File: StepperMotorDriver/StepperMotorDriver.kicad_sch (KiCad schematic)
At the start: 1 part, among them U1 A4988SETTR-T

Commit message: edited schematic
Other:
- note added: "Record to Beat: 0.6"x0.8" 15mm x 20.23mm"
- moved on the sheet: U1
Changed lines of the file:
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@@
 	(generator_version "8.0")
 	(paper "A5")
+	(text "Record to Beat: \n0.6\"x0.8\"\n15mm x 20.23mm"
+		(exclude_from_sim no)
+		(at 185.674 19.812 0)
+		(effects
+			(font
+				(size 1.27 1.27)
+			)
+		)
+	)
 	(symbol
 		(lib_id "Project_Symbols:A4988SETTR-T")
-		(at 83.82 44.45 0)
+		(at 81.28 41.91 0)
 		(unit 1)
 		(exclude_from_sim no)
@@
 		(fields_autoplaced yes)
 		(property "Reference" "U1"
-			(at 102.4318 35.56 0)
+			(at 99.8918 33.02 0)
 			(effects
 				(font
@@
 		)
 		(property "Value" "A4988SETTR-T"
-			(at 102.4318 38.1 0)
+			(at 99.8918 35.56 0)
 			(effects
 				(font
@@
 		)
 		(property "Footprint" "QFN-28_ALM"
-			(at 101.6 41.91 0)
+			(at 99.06 39.37 0)
 			(effects
 				(font
@@
 		)
 		(property "Datasheet" "A4988SETTR-T"
-			(at 101.6 39.37 0)
+			(at 99.06 36.83 0)
 			(effects
 				(font
@@
 		)
 		(property "Description" ""
-			(at 83.82 44.45 0)
+			(at 81.28 41.91 0)
 			(effects
 				(font

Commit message: Edited Schematic
Changed main IC symbol
Added Peripheral components
Assigned footprints
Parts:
- added C1, C2, C3, C4: C, symbol Device:C
- added C5: 100u, symbol Device:C_Polarized
- added R1, R2, R3, R4: R_US, symbol Device:R_US
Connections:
- net at U1.13 (ROSC): now also R2.2
- net at U1.14 (~{SLEEP}): now also R1.2
- net +3.3V: now reaches U1.15 (VDD)
- net +3.3V: now also C4.1, R1.1
- net GND: now reaches U1.18 (GND)
- net GND: now also U1.29 (GND), U1.3 (GND), C1.1, C4.2, C5.2, R2.1, R3.2, R4.2
- net at U1.20 (NC): now also U1.25 (NC), U1.7 (NC)
- net +24V: now reaches U1.22 (VBB1)
- net +24V: now also U1.28 (VBB2), C2.2, C5.1
- net at U1.23 (SENSE1): now also R4.1
- net at U1.27 (SENSE2): now also R3.1
- net at U1.4 (CP1): now also C3.2
- net at U1.5 (CP2): now also C3.1
- net at U1.6 (VCP): now also C2.1
- net at U1.8 (VREG): now also C1.2

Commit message: Updated Schematic
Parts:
- removed R2: R_US, symbol Device:R_US
- added J1: Conn_01x04_Pin, symbol Connector:Conn_01x04_Pin
- added J2: Conn_01x03_Pin, symbol Connector:Conn_01x03_Pin
- C1, C4: value C -> 0.22u
- C2, C3: value C -> 0.1u
- R1: value R_US -> 5k
- R3, R4: value R_US -> 68m
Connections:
- net GND: now also U1.13 (ROSC)
- net at U1.1 (OUT2B): now also J1.4 (Pin_4)
- net MS2: now reaches U1.10 (MS2)
- net MS2: now also J2.2 (Pin_2)
- net MS3: now reaches U1.11 (MS3)
- net MS3: now also J2.3 (Pin_3)
- net at U1.21 (OUT1B): now also J1.2 (Pin_2)
- net at U1.24 (OUT1A): now also J1.1 (Pin_1)
- net at U1.26 (OUT2A): now also J1.3 (Pin_3)
- net MS1: now reaches U1.9 (MS1)
- net MS1: now also J2.1 (Pin_1)
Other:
- moved on the sheet: C4, R1

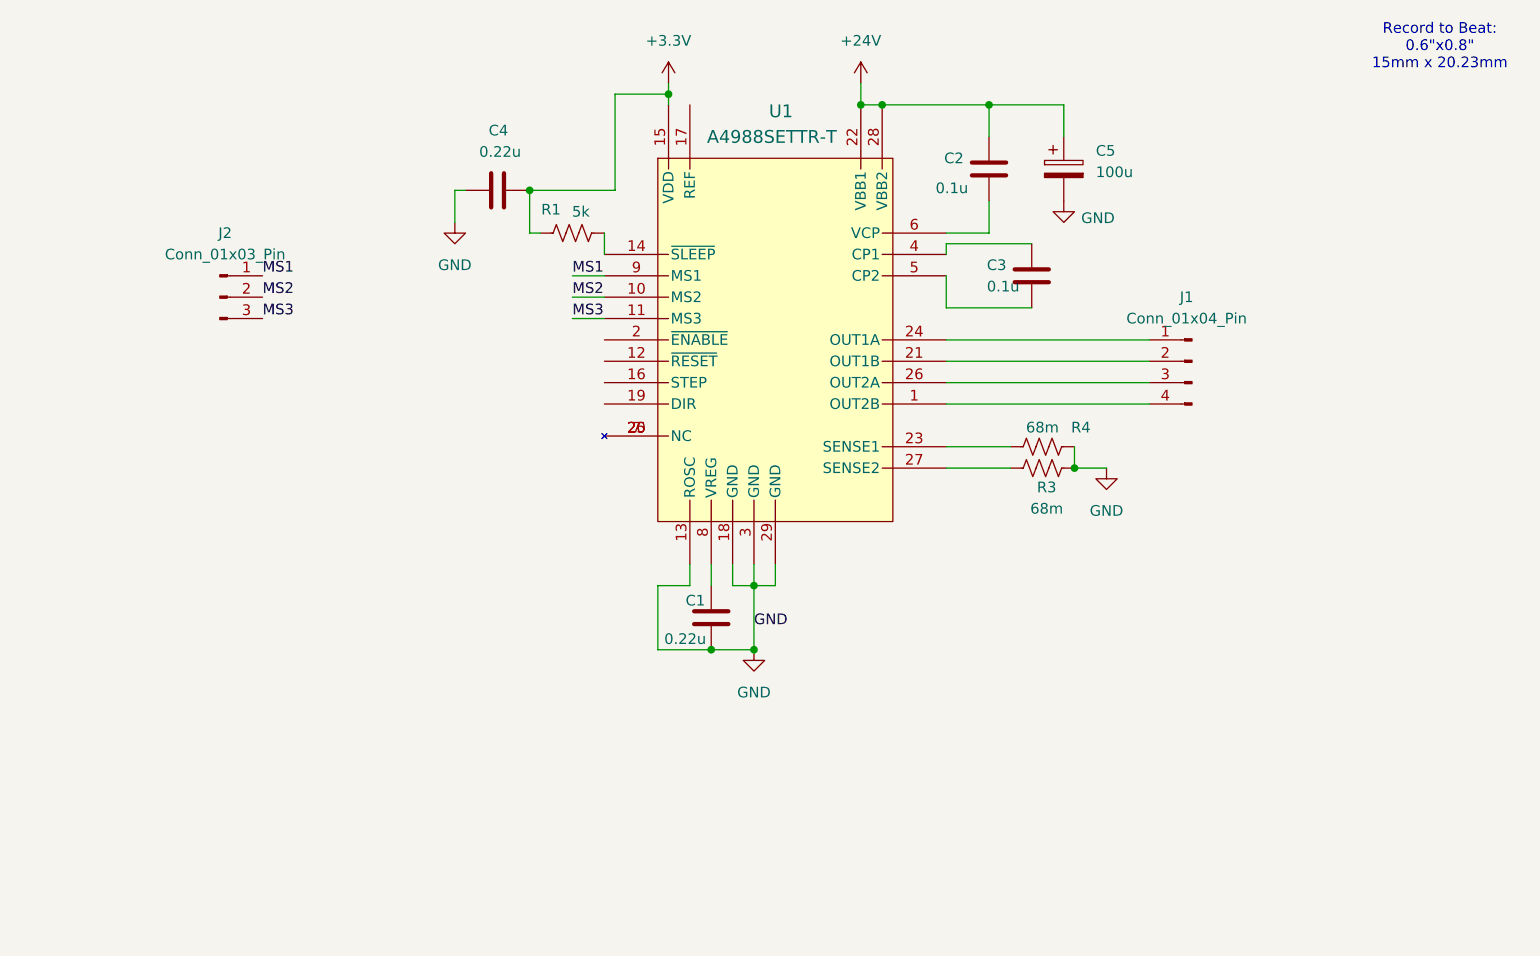
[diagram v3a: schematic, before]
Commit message: COMPLETED schematic and added documentation
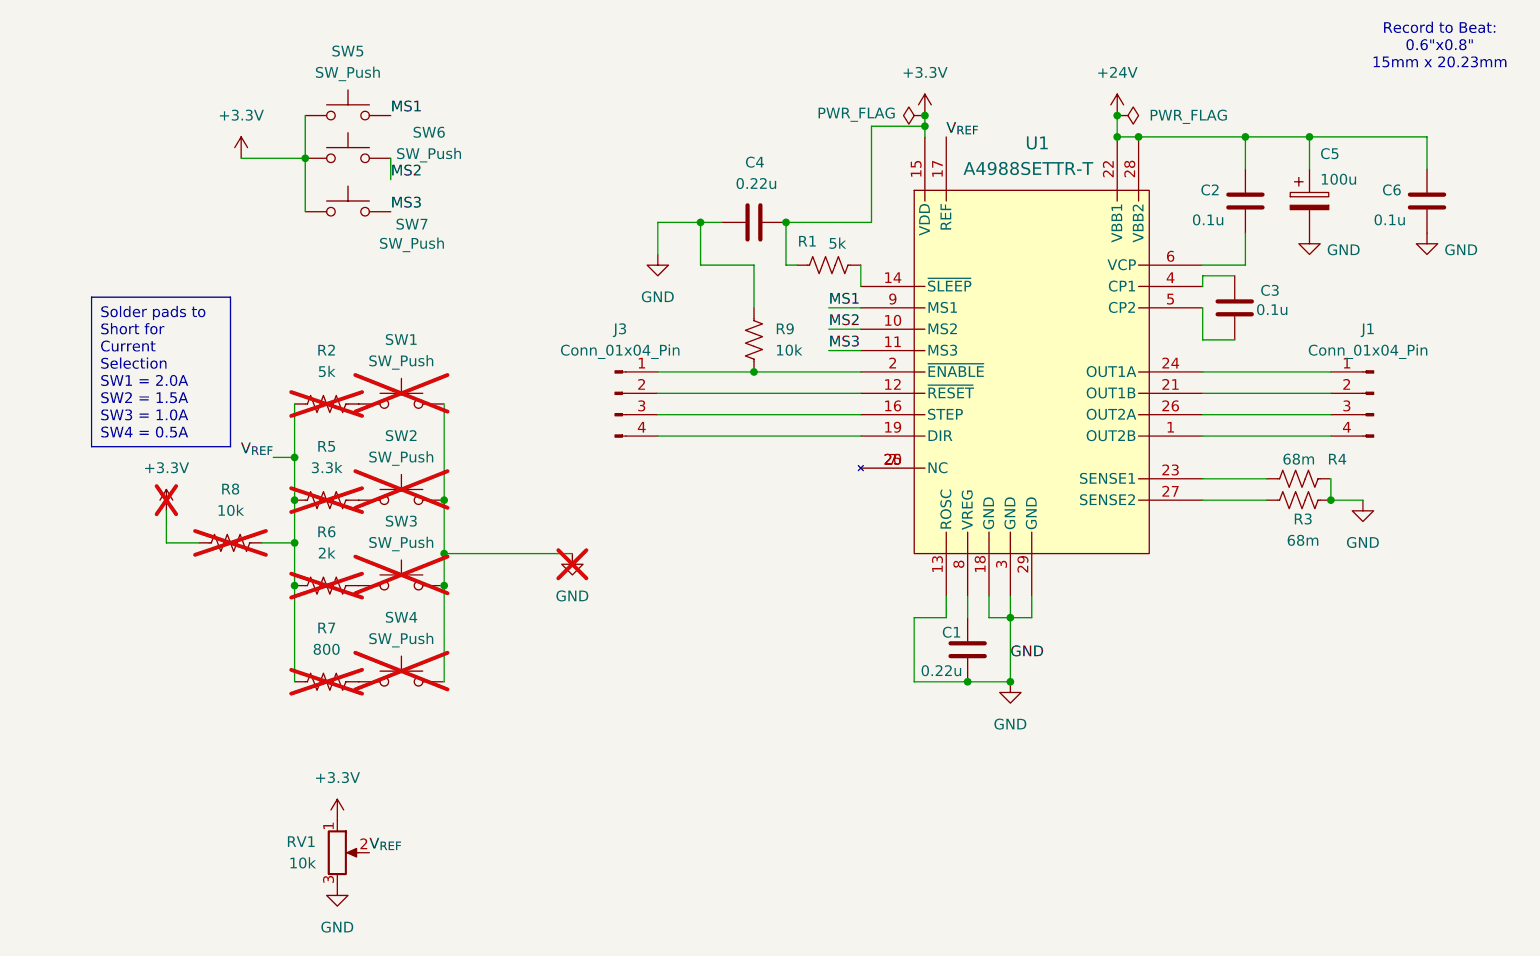
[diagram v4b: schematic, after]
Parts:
- removed J2: Conn_01x03_Pin, symbol Connector:Conn_01x03_Pin
- added C6: 0.1u, symbol Device:C
- added J3: Conn_01x04_Pin, symbol Connector:Conn_01x04_Pin
- added R2: 5k, symbol Device:R_US
- added R5: 3.3k, symbol Device:R_US
- added R6: 2k, symbol Device:R_US
- added R7: 800, symbol Device:R_US
- added R8, R9: 10k, symbol Device:R_US
- added RV1: 10k, Potentiometer_THT:Potentiometer_Bourns_3296P_Horizontal, symbol Device:R_Potentiometer
- added SW1, SW2, SW3, SW4, SW5, SW6, SW7: SW_Push, symbol Switch:SW_Push
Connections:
- net +24V: now also C6.2
- net +3.3V: now also R8.1, RV1.1, SW5.1, SW6.1, SW7.1
- net GND: now also C6.1, R9.2, RV1.3, SW1.2, SW2.2, SW3.2, SW4.2
- net MS1: now also SW5.2
- net MS2: now also SW6.2
- net MS3: now also SW7.2
- net at U1.12 (~{RESET}): now also J3.2 (Pin_2)
- net at U1.16 (STEP): now also J3.3 (Pin_3)
- net V_{REF}: now reaches U1.17 (REF)
- net V_{REF}: now also R2.1, R5.1, R6.1, R7.1, R8.2, RV1.2
- net at U1.19 (DIR): now also J3.4 (Pin_4)
- net at U1.2 (~{ENABLE}): now also J3.1 (Pin_1), R9.1
- new net: R2.2, SW1.1
- new net: R6.2, SW3.1
- new net: R5.2, SW2.1
- new net: R7.2, SW4.1
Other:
- company: (none) -> Aryan Ghosh
- title: (none) -> NanoStep
- moved on the sheet: C1, C2, C3, C4, C5, J1, R1, R3, R4, U1

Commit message: changed schematic, assigned footprints
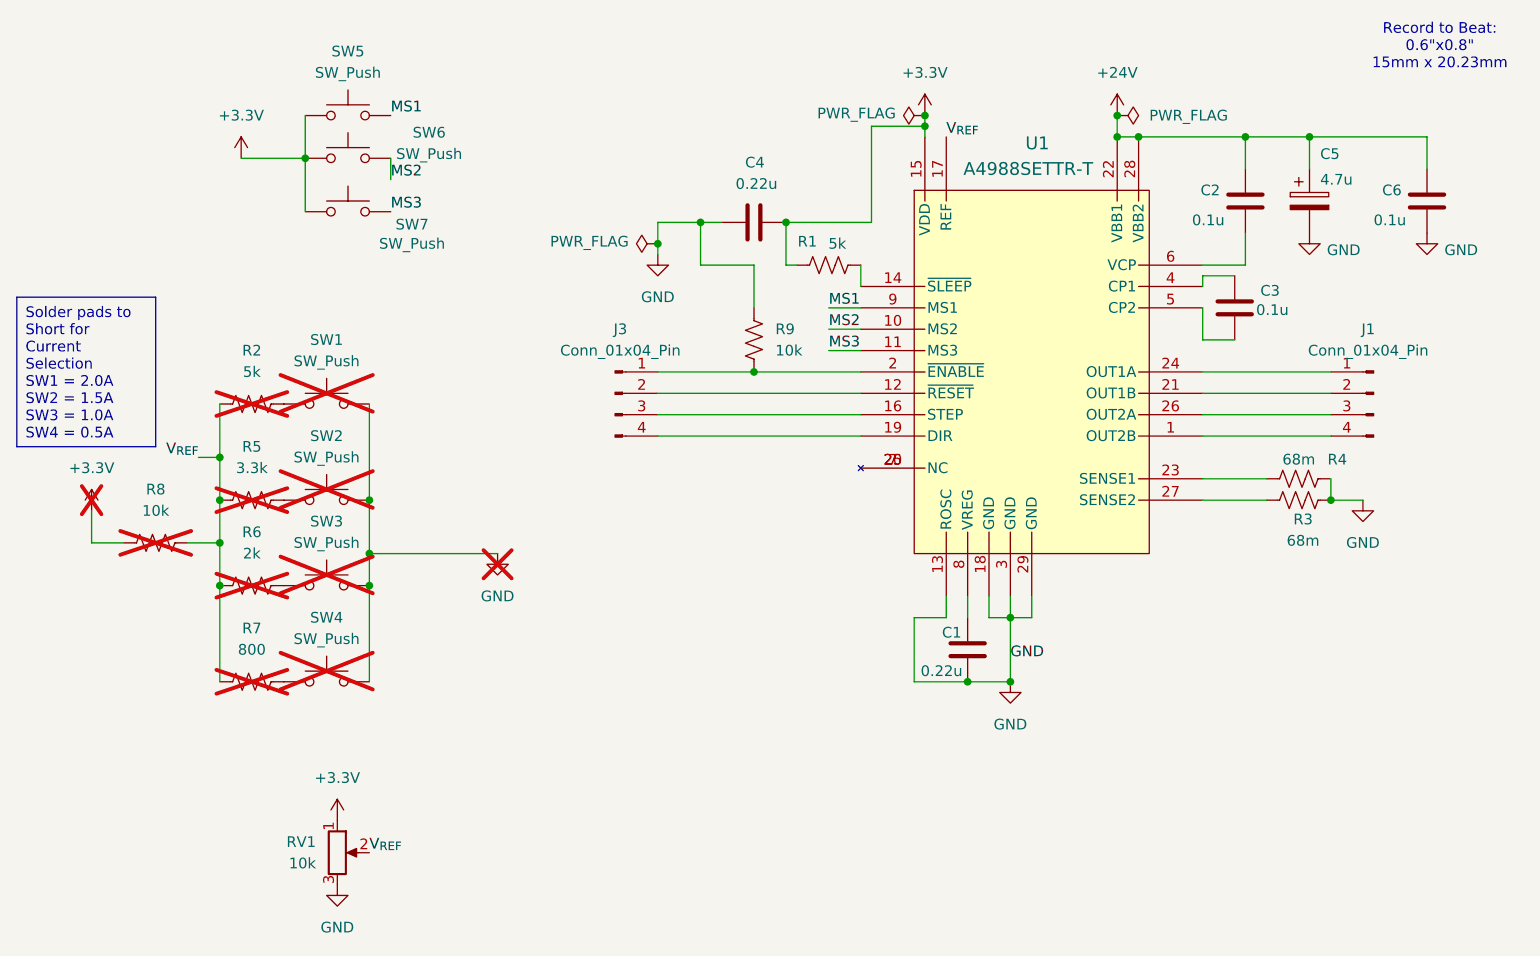
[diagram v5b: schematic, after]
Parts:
- C1, C2, C3, C4, C6: footprint (none) -> Capacitor_SMD:C_0402_1005Metric
- C5: value 100u -> 4.7u; footprint (none) -> Capacitor_SMD:C_0603_1608Metric
- J1: footprint (none) -> Connector_PinHeader_2.54mm:PinHeader_1x04_P2.54mm_Vertical
- J3: footprint (none) -> Connector_PinHeader_1.00mm:PinHeader_1x04_P1.00mm_Vertical_SMD_Pin1Left
- R1, R3, R4, R9: footprint (none) -> Resistor_SMD:R_0402_1005Metric
- RV1: footprint Potentiometer_THT:Potentiometer_Bourns_3296P_Horizontal -> Footprints:POT_3314J
- SW5, SW6, SW7: footprint (none) -> Footprints:Pads to short
- U1: footprint QFN-28_ALM -> Footprints:A4988_QFN-28_ALM
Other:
- moved on the sheet: R2, R5, R6, R7, R8, SW1, SW2, SW3, SW4
